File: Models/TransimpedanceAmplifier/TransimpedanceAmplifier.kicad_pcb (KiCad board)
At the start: 2 copper layers, 107 parts, among them J1 Conn_01x02_Socket, J10 Conn_01x02_Pin, J11 Conn_01x24_Socket, J14 Conn_01x24_Socket, J2 Conn_01x02_Socket, J3 Conn_01x03_Pin, J4 Conn_01x02_Pin, J5 Conn_01x02_Pin, J6 Conn_01x02_Pin, J7 Conn_01x02_Pin, J8 Conn_01x02_Pin, J9 Conn_01x02_Pin, Q1 Q_PNP, Q2 Q_NPN, U1 LM7905, -5V, 5%, U10 DAC81401, U11 ISO7641FM, U12 ISO7641FM, U13 ADS8699, U2 LM7805, 5V, 5%, U3 OPA828, U4 AD8615, U5 OP37GPZ, U6 LM7915, -15V, 5%, U7 LM7815, 15V, 5%, U8 LM7805, 5V, 5%, U9 TLV76133, 3.3V, 1%

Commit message: Finalized all of the text labels
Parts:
- moved R10 6.80 mm to (40.1, 73.9)
- moved R8 6.80 mm to (40.1, 68.6)
- moved D3 6.80 mm to (34.1, 73.9)
- moved R11 6.80 mm to (34.6, 65.9)
- moved R9 6.80 mm to (40.1, 71.2)
- moved D11 3.51 mm to (163.1, 56.6)
- moved U9 3.51 mm to (156.1, 56.5)
- moved C22 3.51 mm to (156.1, 50.8)
- moved C24 3.51 mm to (160.8, 56.7)
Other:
- board text added: "15 V"
- board text added: "27 V"
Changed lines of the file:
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@@
 	(footprint "TwoTerminal:CAPC0805"
 		(layer "F.Cu")
-		(at 160.19 60.12 90)
+		(at 160.84 56.67 90)
 		(property "Reference" "C24"
 			(at -2.71 0 0)
@@
 	(footprint "ThreeTerminal:SOT-23"
 		(layer "F.Cu")
-		(at 34.29 67.14)
+		(at 34.06 73.94)
 		(property "Reference" "D3"
 			(at -0.005 -2.5625 0)
@@
 		(at 120.24 121.85)
 		(property "Reference" "D8"
-			(at 0.01 -1.82 0)
+			(at 3.7 0.02 0)
 			(unlocked yes)
 			(layer "F.SilkS")
@@
 	(footprint "TwoTerminal:RESC0603"
 		(layer "F.Cu")
-		(at 40.335 61.755)
+		(at 40.105 68.555)
 		(property "Reference" "R8"
 			(at 0.0475 -1.385 0)
@@
 	)
 	(footprint "ThreeTerminal:SOT-223"
-		(locked yes)
 		(layer "F.Cu")
-		(at 155.42 59.92 -90)
+		(at 156.07 56.47 -90)
 		(property "Reference" "U9"
 			(at 1.52 4.77 0)
@@
 	(footprint "ThreeTerminal:Bourns_3296Y"
 		(layer "F.Cu")
-		(at 34.88 59.09)
+		(at 34.65 65.89)
 		(property "Reference" "R11"
 			(at 0.0075 -5.85 0)
@@
 	(footprint "TwoTerminal:CAPC0805"
 		(layer "F.Cu")
-		(at 155.42 54.29)
+		(at 156.07 50.84)
 		(property "Reference" "C22"
 			(at 3.16 -0.04 0)
@@
 	(footprint "TwoTerminal:RESC0603"
 		(layer "F.Cu")
-		(at 40.335 67.115)
+		(at 40.105 73.915)
 		(property "Reference" "R10"
 			(at 0.0475 -1.385 0)
@@
 	(footprint "TwoTerminal:RESC0603"
 		(layer "F.Cu")
-		(at 40.335 64.435)
+		(at 40.105 71.235)
 		(property "Reference" "R9"
 			(at 0.0475 -1.385 0)
@@
 	(footprint "TwoTerminal:SOD-123"
 		(layer "F.Cu")
-		(at 162.45 60.1 90)
+		(at 163.1 56.65 90)
 		(property "Reference" "D11"
 			(at 3.45 -0.01 0)
@@
 		(layer "Dwgs.User")
 	)
-	(gr_text "2.5 V"
-		(at 33.73 74.56 90)
-		(layer "User.2")
+	(gr_text "5 V"
+		(at 87.25 66.54 0)
+		(layer "F.SilkS")
 		(effects
 			(font
-				(size 0.8 0.8)
-				(thickness 0.12)
+				(size 1.5 1.5)
+				(thickness 0.3)
+				(bold yes)
 			)
-			(justify left bottom)
+			(justify left top)
+		)
+	)
+	(gr_text "-15 V"
+		(at 116.73 66.47 0)
+		(layer "F.SilkS")
+		(effects
+			(font
+				(size 1.5 1.5)
+				(thickness 0.3)
+				(bold yes)
+			)
+			(justify left top)
+		)
+	)
+	(gr_text "-5 V"
+		(at 104.67 66.59 0)
+		(layer "F.SilkS")
+		(effects
+			(font
+				(size 1.5 1.5)
+				(thickness 0.3)
+				(bold yes)
+			)
+			(justify left top)
+		)
+	)
+	(gr_text "15 V"
+		(at 117.46 118.2 0)
+		(layer "F.SilkS")
+		(effects
+			(font
+				(size 1.5 1.5)
+				(thickness 0.3)
+				(bold yes)
+			)
+			(justify left top)
 		)
 	)
 	(gr_text "3.3 V"
-		(at 148.24 64.08 0)
-		(layer "User.2")
+		(at 158.21 61.27 0)
+		(layer "F.SilkS")
 		(effects
 			(font
-				(size 0.8 0.8)
-				(thickness 0.12)
+				(size 1.5 1.5)
+				(thickness 0.3)
+				(bold yes)
 			)
-			(justify left bottom)
+			(justify left top)
 		)
 	)
-	(gr_text "-1.5 V"
-		(at 31.95 75.53 90)
+	(gr_text "18 V"
+		(at 126.43 52.48 0)
+		(layer "F.SilkS")
+		(effects
+			(font
+				(size 1.5 1.5)
+				(thickness 0.3)
+				(bold yes)
+			)
+			(justify left top)
+		)
+	)
+	(gr_text "5 V"
+		(at 142.38 61.25 0)
+		(layer "F.SilkS")
+		(effects
+			(font
+				(size 1.5 1.5)
+				(thickness 0.3)
+				(bold yes)
+			)
+			(justify left top)
+		)
+	)
+	(gr_text "27 V"
+		(at 128.37 128.26 0)
+		(layer "F.SilkS")
+		(effects
+			(font
+				(size 1.5 1.5)
+				(thickness 0.3)
+				(bold yes)
+			)
+			(justify left top)
+		)
+	)
+	(gr_text "-27 V"
+		(at 93.48 52.68 0)
+		(layer "F.SilkS")
+		(effects
+			(font
+				(size 1.5 1.5)
+				(thickness 0.3)
+				(bold yes)
+			)
+			(justify left top)
+		)
+	)
+	(gr_text "2.5 V"
+		(at 33.5 81.36 90)
 		(layer "User.2")
 		(effects
@@
 		)
 	)
-	(gr_text "5 V"
-		(at 94.17 57.47 0)
+	(gr_text "3.3 V"
+		(at 148.89 60.63 0)
 		(layer "User.2")
 		(effects
@@
 		)
 	)
-	(gr_text "-15 V"
-		(at 123.7075 62.89625 0)
+	(gr_text "-1.5 V"
+		(at 31.72 82.33 90)
 		(layer "User.2")
 		(effects
@@
 	)
 	(gr_text "5 V"
-		(at 135.7175 59.78 0)
+		(at 94.17 57.47 0)
 		(layer "User.2")
 		(effects
@@
 		)
 	)
-	(gr_text "18 V"
-		(at 129.96 53.62 0)
+	(gr_text "-15 V"
+		(at 123.7075 62.89625 0)
 		(layer "User.2")
 		(effects
@@
 		)
 	)
-	(gr_text "-5 V"
-		(at 111.18 63.13375 0)
+	(gr_text "5 V"
+		(at 135.7175 59.78 0)
 		(layer "User.2")
 		(effects
@@
 		)
 	)
-	(gr_text "-27 V"
-		(at 96.87 53.73 0)
+	(gr_text "-5 V"
+		(at 111.18 63.13375 0)
 		(layer "User.2")
 		(effects
@@
 	)
 	(segment
-		(start 162.45 58.32)
-		(end 162.05 57.92)
+		(start 163.1 54.87)
+		(end 162.7 54.47)
 		(width 0.2)
 		(layer "F.Cu")
@@
 	)
 	(segment
-		(start 156.4225 54.29)
-		(end 156.4225 55.5225)
+		(start 157.0725 50.84)
+		(end 157.0725 52.0725)
 		(width 0.2)
 		(layer "F.Cu")
@@
 	)
 	(segment
-		(start 156.4225 55.5225)
-		(end 157.72 56.82)
+		(start 157.0725 52.0725)
+		(end 158.37 53.37)
 		(width 0.2)
 		(layer "F.Cu")
@@
 	)
 	(segment
-		(start 160.0175 59.1175)
-		(end 157.72 56.82)
+		(start 160.6675 55.6675)
+		(end 158.37 53.37)
 		(width 0.2)
 		(layer "F.Cu")
@@
 	)
 	(segment
-		(start 160.19 59.1175)
-		(end 161.655 59.1175)
+		(start 160.84 55.6675)
+		(end 162.305 55.6675)
 		(width 0.2)
 		(layer "F.Cu")
@@
 	)
 	(segment
-		(start 160.19 59.1175)
-		(end 160.0175 59.1175)
+		(start 160.84 55.6675)
+		(end 160.6675 55.6675)
 		(width 0.2)
 		(layer "F.Cu")
@@
 	)
 	(segment
-		(start 162.04 57.91)
-		(end 161.47 57.91)
+		(start 162.69 54.46)
+		(end 162.12 54.46)
 		(width 0.2)
 		(layer "F.Cu")
@@
 	)
 	(segment
-		(start 162.45 58.3225)
-		(end 162.45 58.32)
+		(start 163.1 54.8725)
+		(end 163.1 54.87)
 		(width 0.2)
 		(layer "F.Cu")
@@
 	)
 	(segment
-		(start 162.05 57.92)
-		(end 162.04 57.91)
+		(start 162.7 54.47)
+		(end 162.69 54.46)
 		(width 0.2)
 		(layer "F.Cu")
@@
 	)
 	(segment
-		(start 161.655 59.1175)
-		(end 162.45 58.3225)
+		(start 162.305 55.6675)
+		(end 163.1 54.8725)
 		(width 0.2)
 		(layer "F.Cu")
@@
 	)
 	(via
-		(at 161.47 57.91)
+		(at 162.12 54.46)
 		(size 0.6)
 		(drill 0.3)
@@
 	)
 	(segment
-		(start 154.4175 54.29)
-		(end 154.4175 55.5225)
+		(start 155.0675 50.84)
+		(end 155.0675 52.0725)
 		(width 0.2)
 		(layer "F.Cu")
@@
 	)
 	(segment
-		(start 154.4175 55.5225)
-		(end 153.12 56.82)
+		(start 155.0675 52.0725)
+		(end 153.77 53.37)
 		(width 0.2)
 		(layer "F.Cu")
@@
 	)
 	(segment
-		(start 160.19 61.1225)
-		(end 161.695 61.1225)
+		(start 160.84 57.6725)
+		(end 162.345 57.6725)
 		(width 0.2)
 		(layer "F.Cu")
@@
 	)
 	(segment
-		(start 160.19 61.1225)
-		(end 157.3175 61.1225)
+		(start 160.84 57.6725)
+		(end 157.9675 57.6725)
 		(width 0.2)
 		(layer "F.Cu")
@@
 	)
 	(segment
-		(start 157.3175 61.1225)
-		(end 155.42 63.02)
+		(start 157.9675 57.6725)
+		(end 156.07 59.57)
 		(width 0.2)
 		(layer "F.Cu")
@@
 	)
 	(segment
-		(start 161.695 61.1225)
-		(end 162.45 61.8775)
+		(start 162.345 57.6725)
+		(end 163.1 58.4275)
 		(width 0.2)
 		(layer "F.Cu")

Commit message: Very good developments. Next step is the voltage divider.
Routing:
- net /3.3V_Converter: track 47.7 -> 104.4 mm
- net /5V_Converter: track 25.8 -> 81.4 mm
- net /Power/Batteries/-27V: track 4.63 -> 28.0 mm
- net /-15V: track 46.3 -> 69.2 mm
- net /Power/Batteries/18V: track 3.50 -> 14.9 mm
- net /Power/Batteries/27V: track 10.9 -> 15.5 mm

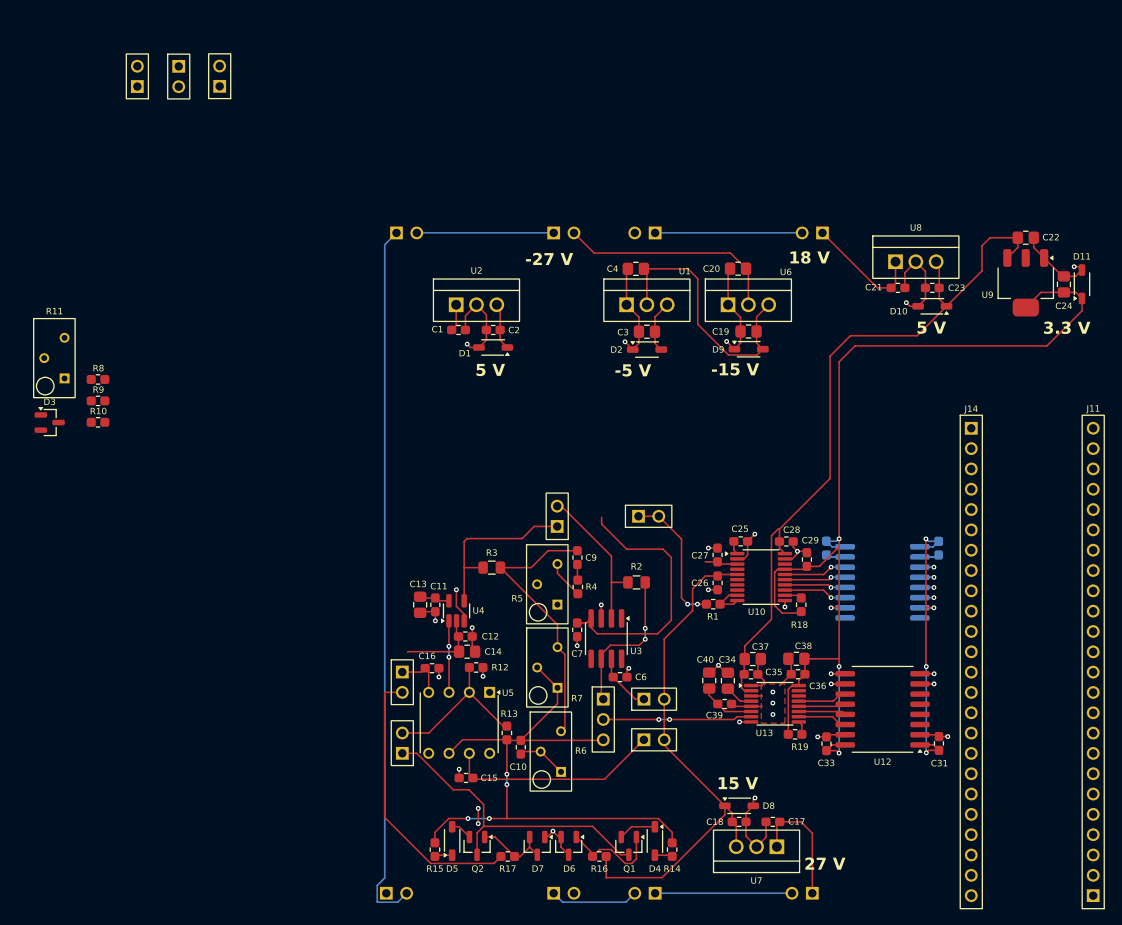
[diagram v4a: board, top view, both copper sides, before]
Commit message: Connected an important power trace
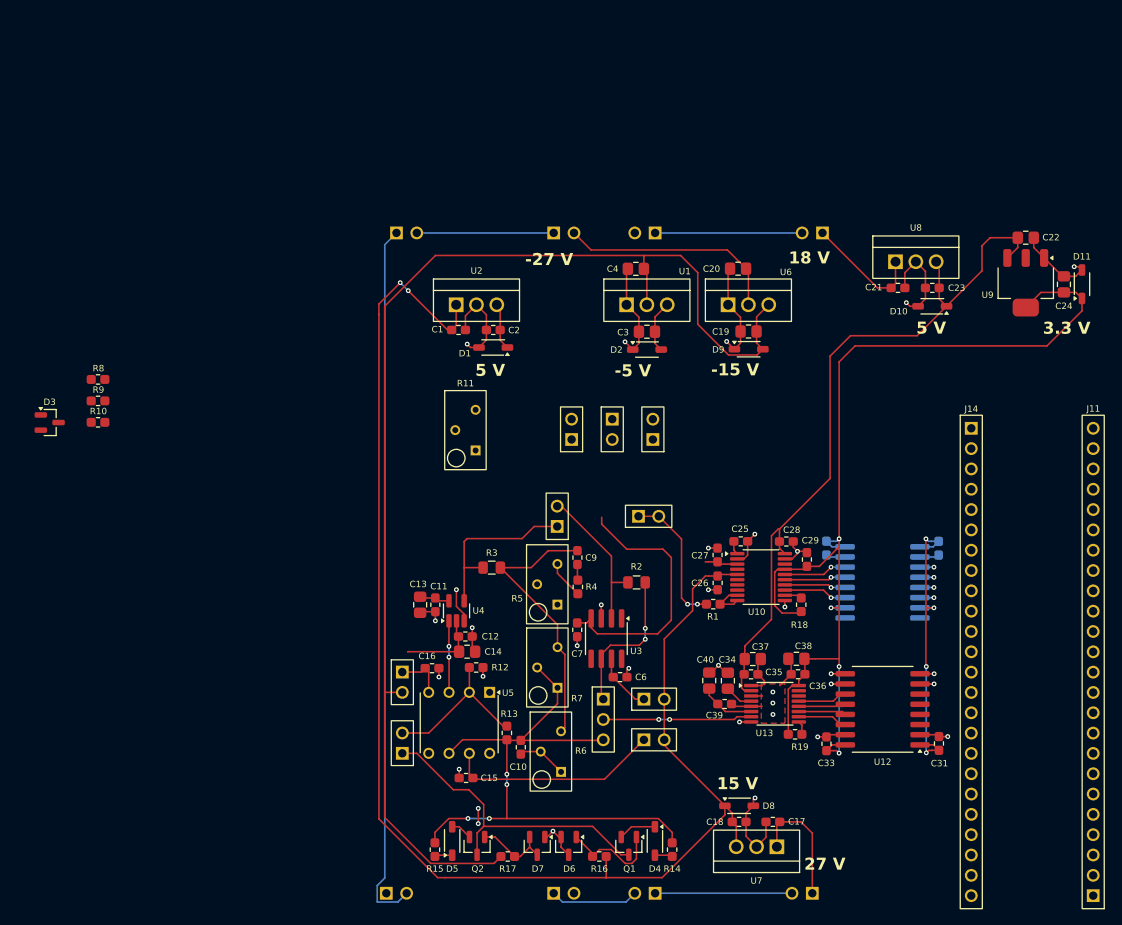
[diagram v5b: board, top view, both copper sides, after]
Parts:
- moved J7 69.9 mm to (99.3, 74.8)
- moved J6 69.9 mm to (104.4, 74.8)
- moved J5 69.9 mm to (109.5, 74.8)
- moved R11 52.2 mm to (86.0, 74.9)
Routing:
- net /15V: track 65.0 -> 173.4 mm, vias 0 -> 2
- net /-15V: track 69.2 -> 155.3 mm
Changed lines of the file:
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@@
 	(footprint "Connector_Custom:PinHeader_1x2"
 		(layer "F.Cu")
-		(at 45.02 30.67 180)
+		(at 99.3 74.79 180)
 		(property "Reference" "J7"
 			(at 0.0025 -3.5625 180)
@@
 	(footprint "Connector_Custom:PinHeader_1x2"
 		(layer "F.Cu")
-		(at 50.19 30.69)
+		(at 104.38 74.79)
 		(property "Reference" "J6"
 			(at 0.0025 -3.5625 0)
@@
 	(footprint "Connector_Custom:PinHeader_1x2"
 		(layer "F.Cu")
-		(at 55.31 30.65 180)
+		(at 109.46 74.79 180)
 		(property "Reference" "J5"
 			(at 0.0025 -3.5625 180)
@@
 	(footprint "ThreeTerminal:Bourns_3296Y"
 		(layer "F.Cu")
-		(at 34.65 65.89)
+		(at 86.03 74.89)
 		(property "Reference" "R11"
 			(at 0.0075 -5.85 0)
@@
 	)
 	(segment
-		(start 102.11 52.75)
-		(end 119.1525 52.75)
+		(start 121.4 54.9975)
+		(end 121.1125 54.71)
 		(width 0.2)
 		(layer "F.Cu")
@@
 	)
 	(segment
-		(start 121.4 54.9975)
-		(end 121.1125 54.71)
+		(start 121.4 59.22)
+		(end 121.4 54.9975)
 		(width 0.2)
 		(layer "F.Cu")
@@
 	)
 	(segment
-		(start 121.4 59.22)
-		(end 121.4 54.9975)
+		(start 118.7725 52.37)
+		(end 121.1125 54.71)
 		(width 0.2)
 		(layer "F.Cu")
@@
 	(segment
 		(start 99.6 50.24)
-		(end 102.11 52.75)
+		(end 101.73 52.37)
 		(width 0.2)
 		(layer "F.Cu")
@@
 	)
 	(segment
-		(start 119.1525 52.75)
-		(end 121.1125 54.71)
+		(start 101.73 52.37)
+		(end 118.7725 52.37)
 		(width 0.2)
 		(layer "F.Cu")
@@
 	)
 	(segment
+		(start 75.22 60.43)
+		(end 75.21 60.42)
+		(width 0.2)
+		(layer "F.Cu")
+		(net 10)
+	)
+	(segment
+		(start 83.79 62.37)
+		(end 84.31 62.37)
+		(width 0.2)
+		(layer "F.Cu")
+		(net 10)
+	)
+	(segment
 		(start 103.62 130.83)
 		(end 103.622833 130.827167)
@@
 	)
 	(segment
+		(start 78.88 57.46)
+		(end 83.79 62.37)
+		(width 0.2)
+		(layer "F.Cu")
+		(net 10)
+	)
+	(segment
 		(start 114.429 94.721)
 		(end 116.025 93.125)
@@
 	)
 	(segment
+		(start 75.22 123.49)
+		(end 75.22 60.43)
+		(width 0.2)
+		(layer "F.Cu")
+		(net 10)
+	)
+	(segment
+		(start 103.622833 130.827167)
+		(end 83.482833 130.827167)
+		(width 0.2)
+		(layer "F.Cu")
+		(net 10)
+	)
+	(segment
 		(start 110.88 108.52)
 		(end 110.88 113.6)
@@
 	)
 	(segment
+		(start 83.48 130.83)
+		(end 82.56 130.83)
+		(width 0.2)
+		(layer "F.Cu")
+		(net 10)
+	)
+	(segment
+		(start 75.21 59.13)
+		(end 77.88 56.46)
+		(width 0.2)
+		(layer "F.Cu")
+		(net 10)
+	)
+	(segment
 		(start 119.38 123.86)
 		(end 119.38 122.7675)
@@
 	)
 	(segment
+		(start 82.56 130.83)
+		(end 75.22 123.49)
+		(width 0.2)
+		(layer "F.Cu")
+		(net 10)
+	)
+	(segment
 		(start 119.88 126.97)
 		(end 119.88 124.36)
@@
 	)
 	(segment
+		(start 75.21 60.42)
+		(end 75.21 59.13)
+		(width 0.2)
+		(layer "F.Cu")
+		(net 10)
+	)
+	(segment
 		(start 110.88 108.52)
 		(end 110.88 101)
@@
 	)
 	(segment
+		(start 83.482833 130.827167)
+		(end 83.48 130.83)
+		(width 0.2)
+		(layer "F.Cu")
+		(net 10)
+	)
+	(via
+		(at 77.88 56.46)
+		(size 0.6)
+		(drill 0.3)
+		(layers "F.Cu" "B.Cu")
+		(net 10)
+	)
+	(via
+		(at 78.88 57.46)
+		(size 0.6)
+		(drill 0.3)
+		(layers "F.Cu" "B.Cu")
+		(net 10)
+	)
+	(segment
+		(start 77.88 56.46)
+		(end 78.88 57.46)
+		(width 0.2)
+		(layer "B.Cu")
+		(net 10)
+	)
+	(segment
 		(start 90.37 59.64)
 		(end 89.95 59.22)
@@
 	(segment
 		(start 115.07 61.648628)
-		(end 115.07 55.96)
+		(end 118.916122 65.49475)
 		(width 0.2)
 		(layer "F.Cu")
@@
 	)
 	(segment
-		(start 122.4915 65.49475)
-		(end 118.916122 65.49475)
+		(start 75.94 107.67)
+		(end 75.94 59.4)
 		(width 0.2)
 		(layer "F.Cu")
@@
 	)
 	(segment
-		(start 115.07 55.96)
-		(end 113.84 54.73)
+		(start 82.28 53.06)
+		(end 108.35 53.06)
+		(width 0.2)
+		(layer "F.Cu")
+		(net 13)
+	)
+	(segment
+		(start 108.35 53.06)
+		(end 112.93 53.06)
+		(width 0.2)
+		(layer "F.Cu")
+		(net 13)
+	)
+	(segment
+		(start 115.07 55.2)
+		(end 115.07 61.648628)
 		(width 0.2)
 		(layer "F.Cu")
@@
 	)
 	(segment
+		(start 118.916122 65.49475)
+		(end 122.4915 65.49475)
+		(width 0.2)
+		(layer "F.Cu")
+		(net 13)
+	)
+	(segment
 		(start 108.71 59.22)
 		(end 108.71 55.1075)
@@
 	)
 	(segment
-		(start 123.2075 64.77875)
-		(end 122.4915 65.49475)
+		(start 108.3325 53.0775)
+		(end 108.35 53.06)
 		(width 0.2)
 		(layer "F.Cu")
@@
 	)
 	(segment
-		(start 118.916122 65.49475)
-		(end 115.07 61.648628)
+		(start 112.93 53.06)
+		(end 115.07 55.2)
 		(width 0.2)
 		(layer "F.Cu")
@@
 	)
 	(segment
-		(start 113.84 54.73)
-		(end 108.3325 54.73)
+		(start 108.3325 54.73)
+		(end 108.3325 53.0775)
+		(width 0.2)
+		(layer "F.Cu")
+		(net 13)
+	)
+	(segment
+		(start 75.94 59.4)
+		(end 82.28 53.06)
 		(width 0.2)
 		(layer "F.Cu")
@@
 		(width 0.2)
 		(layer "F.Cu")
+		(net 13)
+	)
+	(segment
+		(start 122.4915 65.49475)
+		(end 123.2075 64.77875)
+		(width 0.2)
+		(layer "F.Cu")
